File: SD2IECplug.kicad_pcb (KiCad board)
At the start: 2 copper layers, 50 x 49 mm, 44 parts, among them J1 ISP, J2 X6, J3 Aux, J4 IEC, J5 C64-CassettePort, J6 C64-CassettePort, J7 Power, J8 X3, Q1 IRLML2803, Q2 IRLML2803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

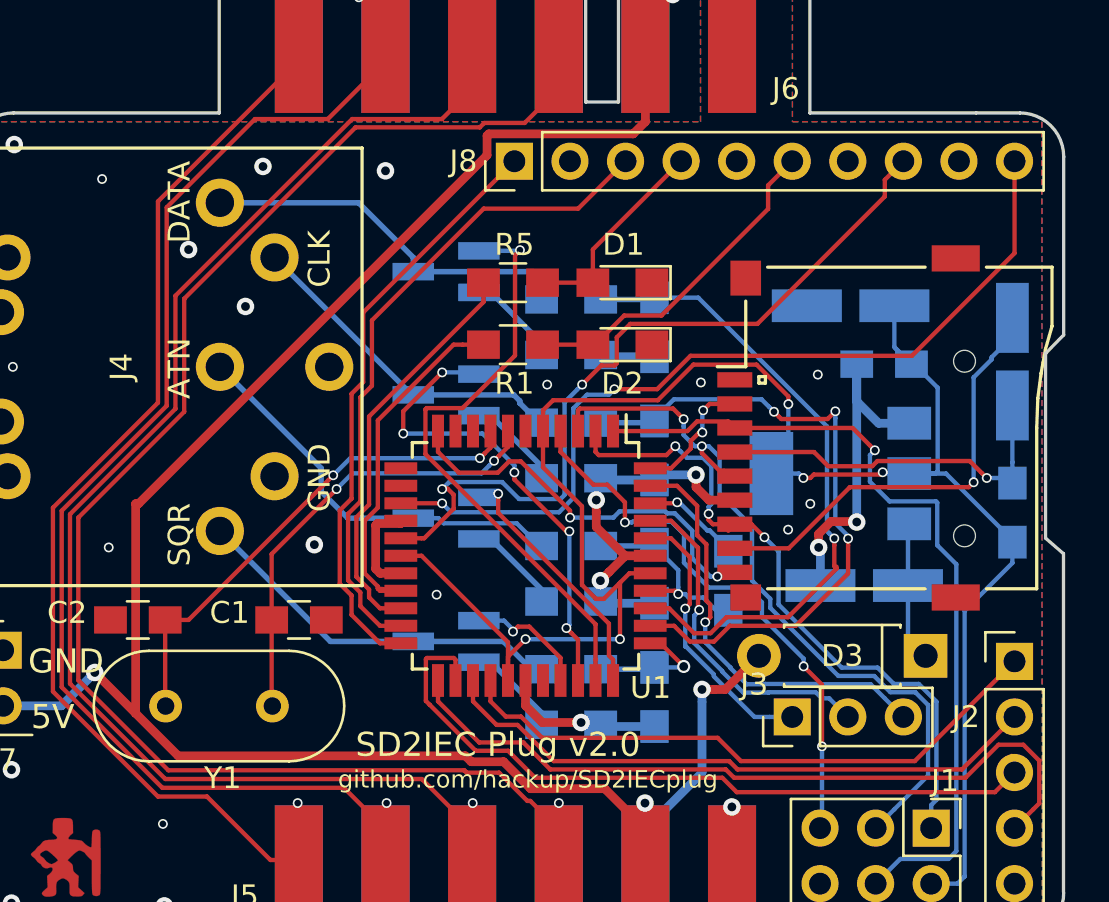
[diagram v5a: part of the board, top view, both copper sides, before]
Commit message: Added mounting hole.
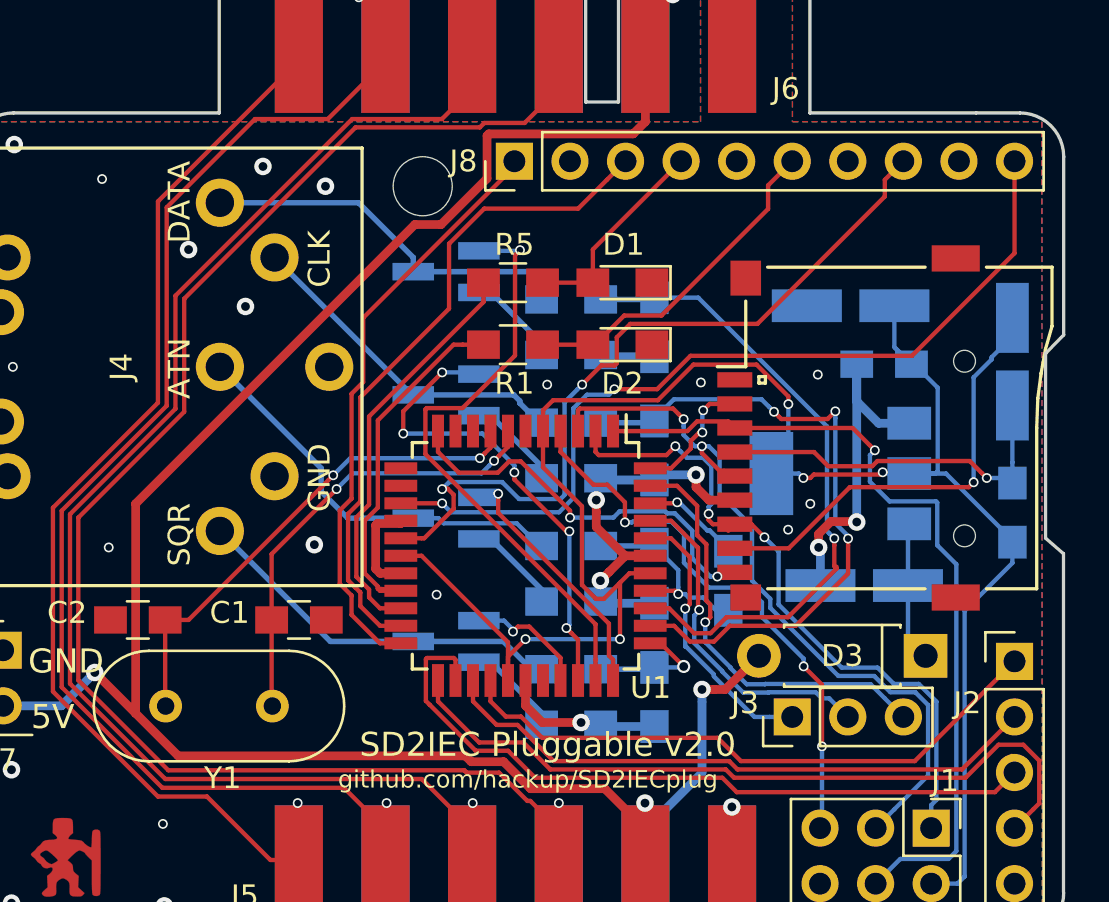
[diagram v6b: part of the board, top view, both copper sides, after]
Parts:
- added MH3: MountingHole, Mounting_Holes:MountingHole_2.7mm_M2.5, F.Cu at (78.7, 105.7)
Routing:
- net Cas-5V: track 100.8 -> 101.4 mm
- net Cas-GND: vias 26 -> 25
- net (no net): vias 0 -> 1
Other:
- board text added: "SD2IEC Pluggable v2.0"
- board text removed: "SD2IEC Plug v2.0"
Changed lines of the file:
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@@
     (thickness 1.6)
     (drawings 37)
-    (tracks 810)
+    (tracks 815)
     (zones 0)
-    (modules 44)
+    (modules 45)
     (nets 57)
   )
@@
     (descr "Through hole straight pin header, 1x03, 2.54mm pitch, single row")
     (tags "Through hole pin header THT 1x03 2.54mm single row")
-    (fp_text reference J3 (at 1.4859 -1.7399 180) (layer F.SilkS)
+    (fp_text reference J3 (at 0.635 -2.159 180) (layer F.SilkS)
       (effects (font (size 1 1) (thickness 0.15)))
     )
@@
     (tags SOT-23)
     (attr smd)
-    (fp_text reference Q4 (at 0 2.5 180) (layer B.SilkS)
+    (fp_text reference Q4 (at -1.2805 2.517 180) (layer B.SilkS)
       (effects (font (size 1 1) (thickness 0.15)) (justify mirror))
     )
@@
     (tags SOT-23)
     (attr smd)
-    (fp_text reference Q1 (at 0 2.5 180) (layer B.SilkS)
+    (fp_text reference Q1 (at -1.217 2.471 180) (layer B.SilkS)
       (effects (font (size 1 1) (thickness 0.15)) (justify mirror))
     )
@@
     (tags SOT-23)
     (attr smd)
-    (fp_text reference Q2 (at 0 2.5 180) (layer B.SilkS)
+    (fp_text reference Q2 (at -1.217 2.506 180) (layer B.SilkS)
       (effects (font (size 1 1) (thickness 0.15)) (justify mirror))
     )
@@
     (tags SOT-23)
     (attr smd)
-    (fp_text reference Q3 (at 0 2.5 180) (layer B.SilkS)
+    (fp_text reference Q3 (at -1.217 2.552 180) (layer B.SilkS)
       (effects (font (size 1 1) (thickness 0.15)) (justify mirror))
     )
@@
     (descr "Through hole straight pin header, 1x05, 2.54mm pitch, single row")
     (tags "Through hole pin header THT 1x05 2.54mm single row")
-    (fp_text reference J2 (at -2.2225 2.54) (layer F.SilkS)
+    (fp_text reference J2 (at -2.159 1.905) (layer F.SilkS)
       (effects (font (size 1 1) (thickness 0.15)))
     )
@@
     )
   )
+  (module Mounting_Holes:MountingHole_2.7mm_M2.5 (layer F.Cu)
+    (at 78.701 105.705)
+    (descr "Mounting Hole 2.7mm, no annular, M2.5")
+    (tags "mounting hole 2.7mm no annular m2.5")
+    (attr virtual)
+    (fp_text reference MH3 (at 0 -3.7) (layer F.SilkS) hide
+      (effects (font (size 1 1) (thickness 0.15)))
+    )
+    (fp_text value MountingHole (at 0 3.7) (layer F.Fab)
+      (effects (font (size 1 1) (thickness 0.15)))
+    )
+    (fp_text user %R (at 0.3 0) (layer F.Fab)
+      (effects (font (size 1 1) (thickness 0.15)))
+    )
+    (fp_circle (center 0 0) (end 2.7 0) (layer Cmts.User) (width 0.15))
+    (fp_circle (center 0 0) (end 2.95 0) (layer F.CrtYd) (width 0.05))
+    (pad 1 np_thru_hole circle (at 0 0) (size 2.7 2.7) (drill 2.7) (layers *.Cu *.Mask))
+  )
   (gr_text GND (at 60.667 127.422) (layer F.SilkS)
     (effects (font (size 1.1 1.1) (thickness 0.2)) (justify left))
@@
   (gr_line (start 96.4 102.354) (end 96.4 91.989) (angle 90) (layer Edge.Cuts) (width 0.15))
   (gr_arc (start 60 104.354) (end 58 104.354) (angle 90) (layer Edge.Cuts) (width 0.15))
-  (gr_text "SD2IEC Plug v2.0" (at 82.1427 131.232) (layer F.SilkS)
+  (gr_text "SD2IEC Pluggable v2.0" (at 84.416 131.232) (layer F.SilkS)
     (effects (font (size 1.1 1.1) (thickness 0.2)))
   )
@@
   (via (at 59.9685 113.96) (size 0.45) (drill 0.3) (layers F.Cu B.Cu) (net 25))
   (via (at 64.35 122.215) (size 0.45) (drill 0.3) (layers F.Cu B.Cu) (net 25))
-  (via (at 77 105) (size 0.8) (drill 0.4) (layers F.Cu B.Cu) (net 25))
+  (via (at 74.256 105.705) (size 0.8) (drill 0.4) (layers F.Cu B.Cu) (net 0))
   (via (at 70.6 111.2) (size 0.8) (drill 0.4) (layers F.Cu B.Cu) (net 25))
   (via (at 71.4 104.8) (size 0.8) (drill 0.4) (layers F.Cu B.Cu) (net 25))
@@
   (segment (start 91.467741 129.273017) (end 91.467741 128.707332) (width 0.4) (layer B.Cu) (net 26))
   (segment (start 88.88 136.5) (end 88.88 135.1) (width 0.4) (layer B.Cu) (net 26))
-  (segment (start 65.580001 120.215997) (end 65.714003 120.215997) (width 0.4) (layer F.Cu) (net 26))
   (segment (start 88.322001 103.311999) (end 88.88 102.754) (width 0.4) (layer F.Cu) (net 26))
   (segment (start 81.721999 103.311999) (end 88.322001 103.311999) (width 0.4) (layer F.Cu) (net 26))
   (segment (start 88.88 102.754) (end 88.88 96.854) (width 0.4) (layer F.Cu) (net 26))
-  (segment (start 65.714003 120.215997) (end 81.641999 104.288001) (width 0.4) (layer F.Cu) (net 26))
-  (segment (start 81.641999 104.288001) (end 81.641999 103.391999) (width 0.4) (layer F.Cu) (net 26))
   (segment (start 81.641999 103.391999) (end 81.721999 103.311999) (width 0.4) (layer F.Cu) (net 26))
+  (segment (start 81.641999 105.354003) (end 81.641999 103.391999) (width 0.4) (layer F.Cu) (net 26))
+  (segment (start 78.340997 107.455001) (end 79.541001 107.455001) (width 0.4) (layer F.Cu) (net 26))
+  (segment (start 65.580001 120.215997) (end 78.340997 107.455001) (width 0.4) (layer F.Cu) (net 26))
+  (segment (start 79.541001 107.455001) (end 81.641999 105.354003) (width 0.4) (layer F.Cu) (net 26))
   (via (at 84.924 133.899) (size 0.45) (drill 0.3) (layers F.Cu B.Cu) (net 27))
   (segment (start 84.92 136.5) (end 84.92 133.903) (width 0.2) (layer B.Cu) (net 27))
@@
   (segment (start 92.933189 132.741023) (end 103.510394 132.741022) (width 0.2) (layer F.Cu) (net 36))
   (segment (start 92.553178 132.361012) (end 92.933189 132.741023) (width 0.2) (layer F.Cu) (net 36))
+  (segment (start 75.980001 111.723123) (end 82.892 104.811124) (width 0.2) (layer F.Cu) (net 37))
+  (segment (start 75.449966 115.190634) (end 75.980001 114.660599) (width 0.2) (layer F.Cu) (net 37))
+  (segment (start 75.449966 125.295966) (end 75.449966 124.410337) (width 0.2) (layer F.Cu) (net 37))
+  (segment (start 74.909958 120.52167) (end 75.449966 119.981662) (width 0.2) (layer F.Cu) (net 37))
+  (segment (start 82.892 104.811124) (end 82.892 104.562) (width 0.2) (layer F.Cu) (net 37))
   (segment (start 77.7 126.596) (end 76.75 126.596) (width 0.2) (layer F.Cu) (net 37))
   (segment (start 76.75 126.596) (end 75.449966 125.295966) (width 0.2) (layer F.Cu) (net 37))
-  (segment (start 75.449966 125.295966) (end 75.449966 124.410337) (width 0.2) (layer F.Cu) (net 37))
   (segment (start 75.449966 124.410337) (end 74.909957 123.870325) (width 0.2) (layer F.Cu) (net 37))
+  (segment (start 75.980001 114.660599) (end 75.980001 111.723123) (width 0.2) (layer F.Cu) (net 37))
+  (segment (start 75.449966 119.981662) (end 75.449966 115.190634) (width 0.2) (layer F.Cu) (net 37))
   (segment (start 74.909957 123.870325) (end 74.909958 120.52167) (width 0.2) (layer F.Cu) (net 37))
-  (segment (start 75.449966 115.190634) (end 75.980001 114.660599) (width 0.2) (layer F.Cu) (net 37))
-  (segment (start 75.449966 119.981662) (end 75.449966 115.190634) (width 0.2) (layer F.Cu) (net 37))
-  (segment (start 74.909958 120.52167) (end 75.449966 119.981662) (width 0.2) (layer F.Cu) (net 37))
-  (segment (start 75.980001 111.473999) (end 82.892 104.562) (width 0.2) (layer F.Cu) (net 37))
-  (segment (start 75.980001 114.660599) (end 75.980001 111.473999) (width 0.2) (layer F.Cu) (net 37))
+  (segment (start 87.122001 105.411999) (end 87.972 104.562) (width 0.2) (layer F.Cu) (net 38))
   (segment (start 76.75 125.796) (end 75.849977 124.895977) (width 0.2) (layer F.Cu) (net 38))
-  (segment (start 76.380012 114.826288) (end 76.380012 111.835988) (width 0.2) (layer F.Cu) (net 38))
-  (segment (start 76.380012 111.835988) (end 81.487999 106.728001) (width 0.2) (layer F.Cu) (net 38))
-  (segment (start 75.849977 115.356323) (end 76.380012 114.826288) (width 0.2) (layer F.Cu) (net 38))
+  (segment (start 75.849977 124.895977) (end 75.849977 124.272933) (width 0.2) (layer F.Cu) (net 38))
+  (segment (start 75.289968 123.712919) (end 75.289968 120.679076) (width 0.2) (layer F.Cu) (net 38))
+  (segment (start 75.849977 115.356323) (end 79.905519 111.300781) (width 0.2) (layer F.Cu) (net 38))
+  (segment (start 75.289968 120.679076) (end 75.849977 120.119067) (width 0.2) (layer F.Cu) (net 38))
   (segment (start 75.849977 120.119067) (end 75.849977 115.356323) (width 0.2) (layer F.Cu) (net 38))
-  (segment (start 75.289968 120.679076) (end 75.849977 120.119067) (width 0.2) (layer F.Cu) (net 38))
-  (segment (start 75.289967 123.712921) (end 75.289968 120.679076) (width 0.2) (layer F.Cu) (net 38))
-  (segment (start 75.849977 124.272933) (end 75.289967 123.712921) (width 0.2) (layer F.Cu) (net 38))
-  (segment (start 75.849977 124.895977) (end 75.849977 124.272933) (width 0.2) (layer F.Cu) (net 38))
+  (segment (start 81.512539 106.728001) (end 85.805999 106.728001) (width 0.2) (layer F.Cu) (net 38))
+  (segment (start 79.905519 111.300781) (end 79.905519 108.335021) (width 0.2) (layer F.Cu) (net 38))
+  (segment (start 75.617417 124.040372) (end 75.289968 123.712919) (width 0.2) (layer F.Cu) (net 38))
+  (segment (start 75.829977 124.252932) (end 75.617417 124.040372) (width 0.2) (layer F.Cu) (net 38))
+  (segment (start 75.849977 124.272933) (end 75.829977 124.252932) (width 0.2) (layer F.Cu) (net 38))
   (segment (start 77.7 125.796) (end 76.75 125.796) (width 0.2) (layer F.Cu) (net 38))
-  (segment (start 85.805999 106.728001) (end 87.972 104.562) (width 0.2) (layer F.Cu) (net 38))
-  (segment (start 81.487999 106.728001) (end 85.805999 106.728001) (width 0.2) (layer F.Cu) (net 38))
+  (segment (start 85.805999 106.728001) (end 87.122001 105.411999) (width 0.2) (layer F.Cu) (net 38))
+  (segment (start 79.905519 108.335021) (end 81.512539 106.728001) (width 0.2) (layer F.Cu) (net 38))
   (via (at 79.59 119.548) (size 0.45) (drill 0.3) (layers F.Cu B.Cu) (net 39))
   (segment (start 79.607001 119.530999) (end 79.59 119.548) (width 0.2) (layer F.Cu) (net 39))

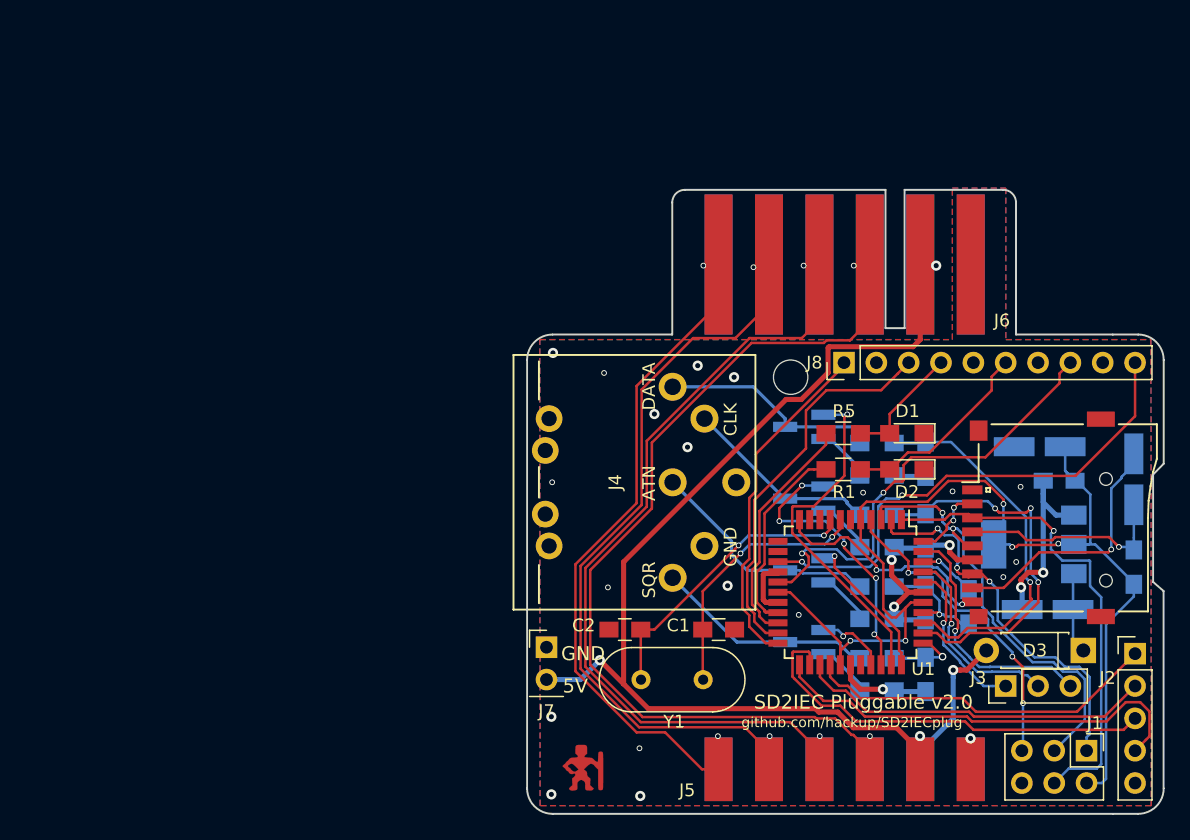
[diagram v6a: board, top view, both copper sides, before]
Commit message: Increased motor line track width.
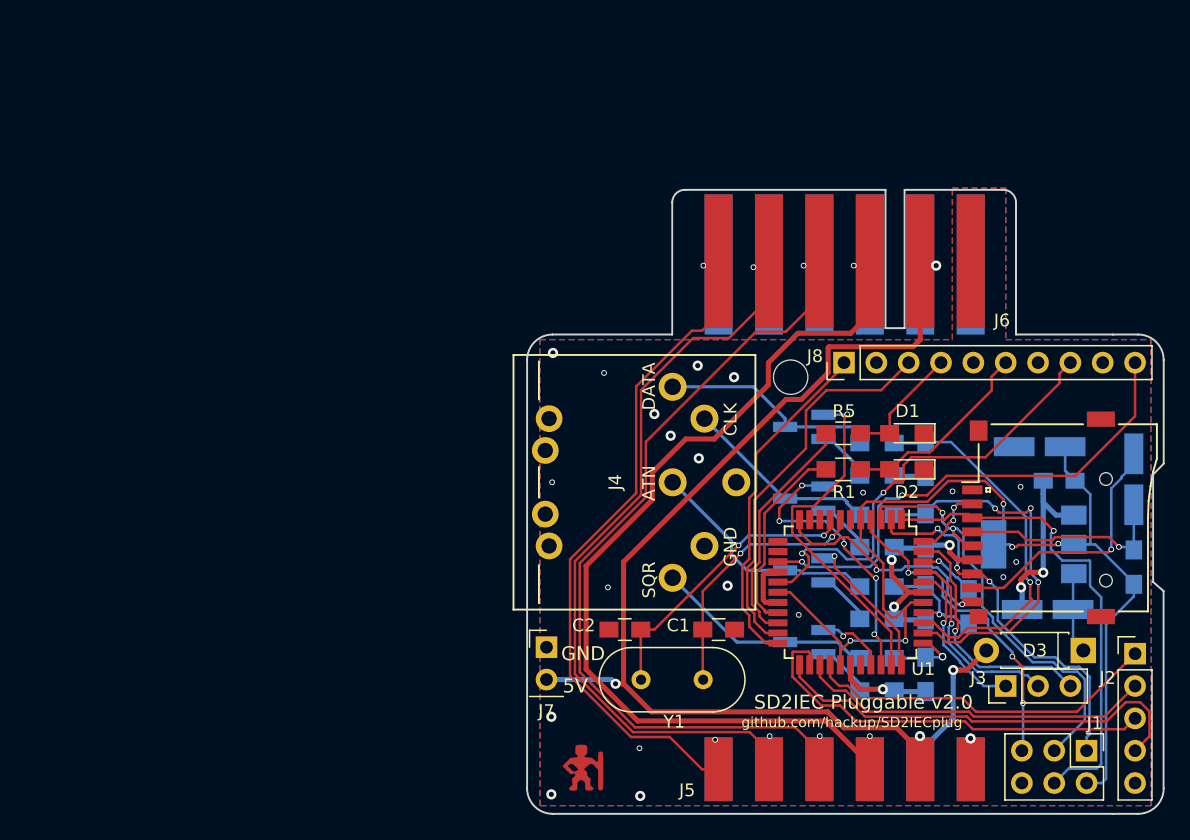
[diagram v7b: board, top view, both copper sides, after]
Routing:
- net Cas-Read: track 71.9 -> 69.2 mm
- net Cas-5V: track 101.4 -> 100.2 mm
- net Cas-Sense: track 58.7 -> 60.0 mm
- net Cas-Write: track 66.6 -> 67.5 mm
- net Cas-GND: vias 25 -> 26
